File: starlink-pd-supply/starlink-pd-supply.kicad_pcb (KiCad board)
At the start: 2 copper layers, 80 parts, among them J1 USB_C_Receptacle, J2 USB_C_Receptacle, Q1 PSMN014-80YL, Q2 PSMN014-80YL, Q3 PSMN014-80YL, U1 CDSOT23-0502B, U10 LT3757, U2 CDSOT23-0502B, U3 PTN5110, U4 PTN5110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

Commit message: WIP
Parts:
- removed R21, R23: 12.7k 1%, Resistor_SMD:R_0805_2012Metric
- removed R22, R29: 165k 1%, Resistor_SMD:R_0805_2012Metric
- added D5: LED, LED_SMD:LED_0805_2012Metric, F.Cu at (100.6, 103.5)
- added H1: MountingHole, MountingHole:MountingHole_4mm_Pad_Via, F.Cu at (108.3, 118.9)
- added H2: MountingHole, MountingHole:MountingHole_4mm_Pad_Via, F.Cu at (48.3, 118.9)
- added H3: MountingHole, MountingHole:MountingHole_4mm_Pad_Via, F.Cu at (108.3, 38.9)
- added H4: MountingHole, MountingHole:MountingHole_4mm_Pad_Via, F.Cu at (48.3, 38.9)
- R20, R28: value 165k 1% -> 10k
- moved C18 192.2 mm to (53.9, 74.8), turned to 90 degrees
- moved R31 190.1 mm to (50.6, 85.8), turned to -90 degrees
- moved R32 189.6 mm to (55.9, 74.8), turned to 90 degrees
- moved C25 178.5 mm to (53.7, 94.1), turned to 90 degrees
- moved C12 177.4 mm to (55.2, 54.4), turned to -90 degrees
- moved R27 174.3 mm to (51.9, 74.8), turned to -90 degrees
- moved R10 168.7 mm to (81.9, 46.8)
- moved R13 167.0 mm to (79.1, 48.8), turned to 180 degrees
- moved R20 165.2 mm to (100.6, 105.6)
- moved R14 164.9 mm to (68.4, 49.1)
- moved C20 163.3 mm to (55.2, 83.6)
- moved R33 163.1 mm to (57.9, 74.8), turned to -90 degrees
- moved R8 162.5 mm to (57.4, 46.9)
- moved R18 161.2 mm to (95.4, 76.3), turned to 90 degrees
- moved R12 160.8 mm to (54.7, 48.9), turned to 180 degrees
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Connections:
- net Net-(D4-Pad2) renamed /BOOST_SW
- net Net-(R12-Pad1) renamed /EN_SINK_A
- net Net-(R13-Pad1) renamed /EN_SINK_B
- J1 pad A5: Net-(J1-PadA5) -> /CC1_A
- J1 pad B5: Net-(J1-PadB5) -> /CC2_A
- J2 pad A5: Net-(J2-PadA5) -> /CC1_B
- J2 pad B5: Net-(J2-PadB5) -> /CC2_B
- R20 pad 1: Net-(R20-Pad1) -> GND
- R20 pad 2: /VBUS_A_SW -> Net-(D5-Pad2)
- R28 pad 1: Net-(R28-Pad1) -> /~{OUT_EN}
- R28 pad 2: /VBUS_OR -> +3V3
- U1 pad 1: Net-(J1-PadB5) -> /CC1_A
- U1 pad 2: Net-(J1-PadA5) -> /CC2_A
- U10 pad 9: Net-(R28-Pad1) -> /~{OUT_EN}
- U2 pad 1: Net-(J2-PadB5) -> /CC1_B
- U2 pad 2: Net-(J2-PadA5) -> /CC2_B
- U3 pad 13: Net-(J1-PadA5) -> /CC1_A
- U3 pad 14: Net-(J1-PadB5) -> /CC2_A
- U4 pad 13: Net-(J2-PadA5) -> /CC1_B
- U4 pad 14: Net-(J2-PadB5) -> /CC2_B
- U5 pad 7: /OUT_EN -> /~{OUT_EN}
- U9 pad 10: unconnected-(U9-Pad10) -> GND
- U9 pad 11: unconnected-(U9-Pad11) -> GND
- U9 pad 12: unconnected-(U9-Pad12) -> GND
- U9 pad 13: unconnected-(U9-Pad13) -> GND
- U9 pad 14: Net-(R20-Pad1) -> GND
- U9 pad 6: unconnected-(U9-Pad6) -> GND
- U9 pad 8: unconnected-(U9-Pad8) -> GND
- U9 pad 9: Net-(R22-Pad1) -> GND
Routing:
- net +3V3: track 0.00 -> 174.2 mm, vias 0 -> 11
- net /TCPC_ALERT_N: track 0.00 -> 112.1 mm, vias 0 -> 3
- net /TCPC_SCL: track 0.00 -> 106.4 mm, vias 0 -> 3
- net /TCPC_SDA: track 0.00 -> 99.9 mm, vias 0 -> 3
- net /~{OUT_EN}: track 0.00 -> 50.4 mm, vias 0 -> 2
- net +48V: track 0.00 -> 35.6 mm, vias 0 -> 2
- net /VBUS_OR: track 0.00 -> 30.4 mm, vias 0 -> 2
- net /IND_G: track 0.00 -> 27.7 mm, vias 0 -> 2
- net /EN_SINK_B: track 0.00 -> 19.3 mm, vias 0 -> 2
- net /EN_SINK_A: track 0.00 -> 18.6 mm, vias 0 -> 2
- net /IND_R: track 0.00 -> 17.1 mm, vias 0 -> 2
- net /CC2_B: track 0.00 -> 16.8 mm, vias 0 -> 1
- net /VBUS_B_SW: track 0.00 -> 16.7 mm
- net /CC2_A: track 0.00 -> 15.3 mm, vias 0 -> 1
- net /IND_B: track 0.00 -> 14.1 mm, vias 0 -> 2
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- added copper zone on F.Cu, net +3V3
- added copper zone on F.Cu, net +48V
- added copper zone on F.Cu, net /3V3_SW
- added copper zone on F.Cu, net /BOOST_SW
- added copper zone on F.Cu, net /VBUS_A
- added copper zone on F.Cu, net /VBUS_A_SW
- added copper zone on F.Cu, net /VBUS_B
- added copper zone on F.Cu, net /VBUS_B_SW
- added copper zone on F.Cu, net /VBUS_OR
- added copper zone on B.Cu, net GND
- added copper zone on F.Cu, net GND
- added copper zone on In1.Cu, net GND
- added copper zone on In2.Cu, net GND
- added copper zone on F.Cu, net Net-(Q3-Pad1)
- added copper zone on F.Cu, net Net-(R16-Pad1)
- added copper zone on F.Cu, net Net-(R17-Pad1)
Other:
- board outline added: 70 x 90 mm
- copper layers 2 -> 4

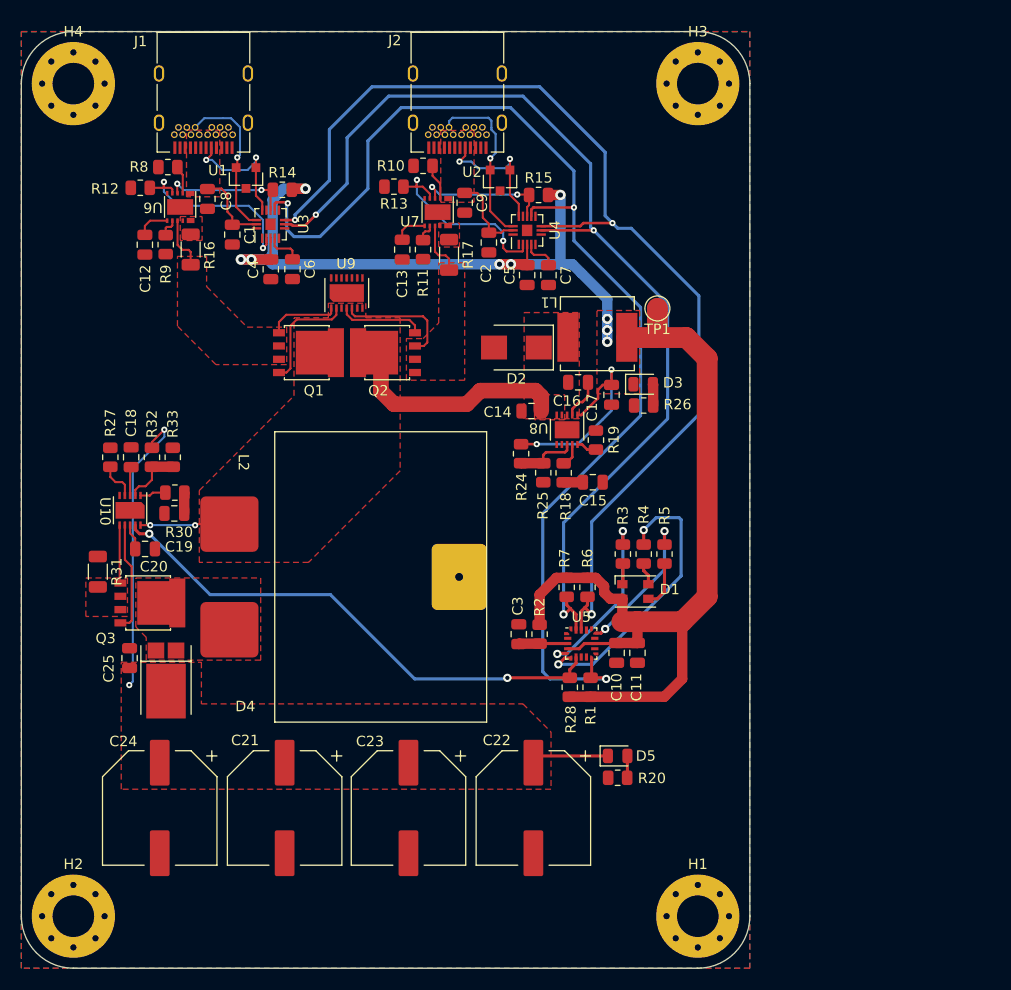
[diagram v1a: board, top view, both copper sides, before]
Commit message: Dishy supply rev 1 complete
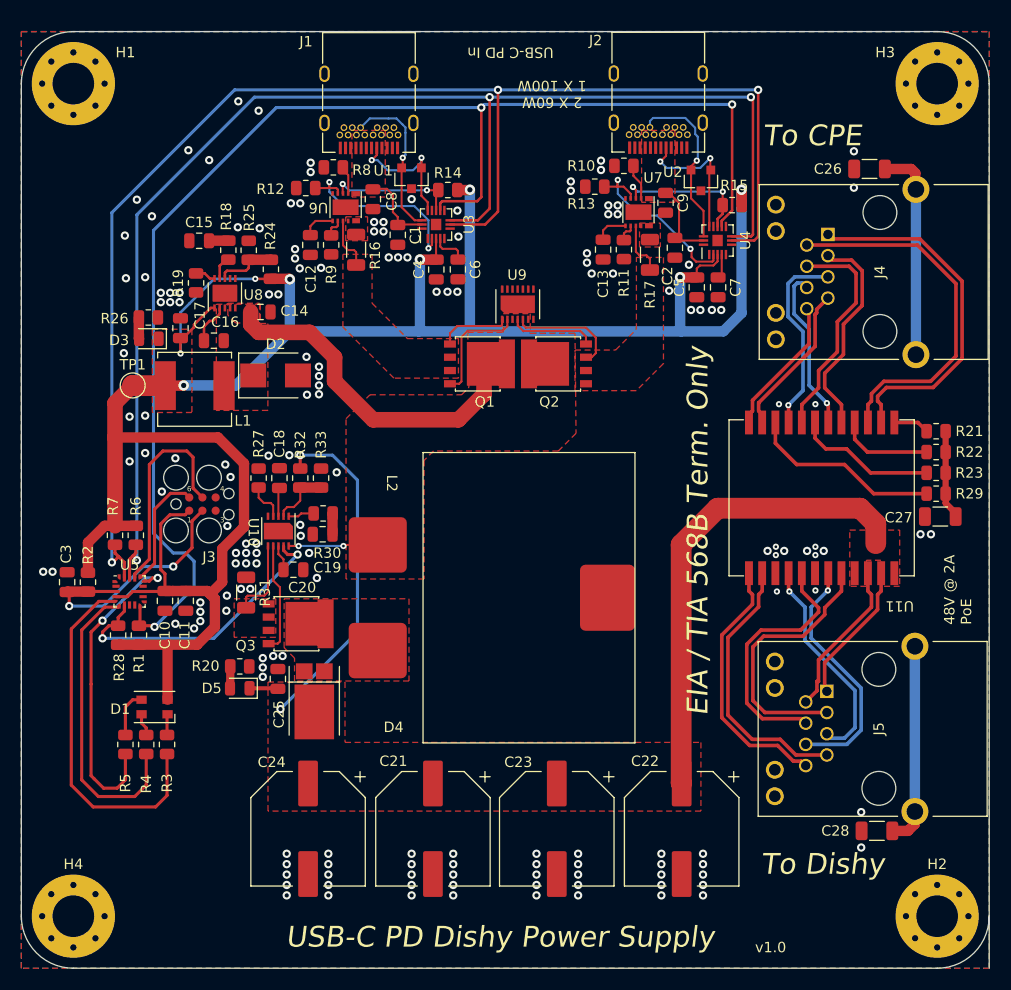
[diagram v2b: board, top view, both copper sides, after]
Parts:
- added C26: 1000p 2kV, Capacitor_SMD:C_1206_3216Metric, F.Cu at (124.8, 47.1)
- added C27: 1000p 2kV, Capacitor_SMD:C_1206_3216Metric, F.Cu at (131.6, 80.5)
- added C28: 1000p 2kV, Capacitor_SMD:C_1206_3216Metric, F.Cu at (125.5, 110.7)
- added J3: TC2030-SWD, Custom:TC2030-IDC-FP, F.Cu at (60.7, 79.3)
- added J4: RJE59-188-54A1, Custom:RJE59-188-54A1, F.Cu at (125.8, 57.0)
- added J5: RJE59-188-54A1, Custom:RJE59-188-54A1, F.Cu at (125.7, 100.9)
- added R21: 75, Resistor_SMD:R_0805_2012Metric, F.Cu at (131.2, 72.3)
- added R22: 75, Resistor_SMD:R_0805_2012Metric, F.Cu at (131.2, 74.3)
- added R23: 75, Resistor_SMD:R_0805_2012Metric, F.Cu at (131.2, 76.3)
- added R29: 75, Resistor_SMD:R_0805_2012Metric, F.Cu at (131.2, 78.3)
- added U11: 7490220123, Custom:7490220123, F.Cu at (120.2, 78.7)
- moved H1 100.0 mm to (48.3, 38.9)
- moved H2 83.0 mm to (131.3, 118.9)
- moved H4 80.0 mm to (48.3, 118.9)
- moved R5 54.9 mm to (53.3, 102.4), turned to -90 degrees
- moved R4 51.2 mm to (55.3, 102.4), turned to 90 degrees
- moved TP1 51.0 mm to (54.0, 67.9), turned to 0 degrees
- moved R26 48.3 mm to (55.5, 61.4), turned to 180 degrees
- moved D3 47.7 mm to (55.6, 63.4), turned to 180 degrees
- moved D1 47.5 mm to (56.1, 98.8), turned to 180 degrees
- moved R3 47.5 mm to (57.3, 102.4), turned to 90 degrees
- moved C15 44.4 mm to (60.4, 54.0), turned to 180 degrees
- moved R6 43.7 mm to (54.3, 82.3)
- moved R7 43.7 mm to (52.3, 82.3)
- moved C10 43.7 mm to (57.1, 88.6)
- moved C11 43.7 mm to (59.1, 88.6)
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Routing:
- net +3V3: track 174.2 -> 225.4 mm, vias 11 -> 8
- net +48V: track 35.6 -> 82.2 mm
- net /TCPC_SDA: track 99.9 -> 138.6 mm
- net /CPE_1_N: track 0.00 -> 35.4 mm
- net /CPE_1_P: track 0.00 -> 34.5 mm
- net /Dishy_4_P: track 0.00 -> 26.1 mm
- net /Dishy_2_P: track 0.00 -> 25.6 mm
- net /Dishy_4_N: track 0.00 -> 25.2 mm
- net /TCPC_SCL: track 106.4 -> 131.3 mm
- net /Dishy_2_N: track 0.00 -> 24.7 mm
- net /Dishy_3_N: track 0.00 -> 23.6 mm, vias 0 -> 1
- net /~{OUT_EN}: track 50.4 -> 28.6 mm
- net /CPE_2_N: track 0.00 -> 21.5 mm
- net /Dishy_3_P: track 0.00 -> 20.8 mm, vias 0 -> 1
- net /SWDCLK: track 0.00 -> 20.7 mm
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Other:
- board size 70 x 90 mm -> 93 x 90 mm
- board text added: "2 X 60W 1 X 100W"
- board text added: "48V @ 2A PoE"
- board text added: "EIA / TIA 568B Term. Only"
- board text added: "To CPE"
- board text added: "To Dishy"
- board text added: "USB-C PD Dishy Power Supply"
- board text added: "USB-C PD In"
- board text added: "v1.0"
